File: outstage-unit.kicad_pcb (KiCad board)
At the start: 2 copper layers, 100 x 220 mm, 76 parts, among them J101 Conn_01x06_Socket, M101 Fan, Q201 DNLS350E, Q202 DPLS350E, Q203 TIP41C, Q204 TIP42C, Q301 DNLS350E, Q302 DPLS350E, Q303 TIP41C, Q304 TIP42C, Q401 DNLS350E, Q402 DPLS350E, Q403 TIP41C, Q404 TIP42C, Q501 DNLS350E, Q502 DPLS350E, Q503 TIP41C, Q504 TIP42C, Q601 DNLS350E, Q602 DPLS350E, Q603 TIP41C, Q604 TIP42C, Q701 DNLS350E, Q702 DPLS350E, Q703 TIP41C, Q704 TIP42C

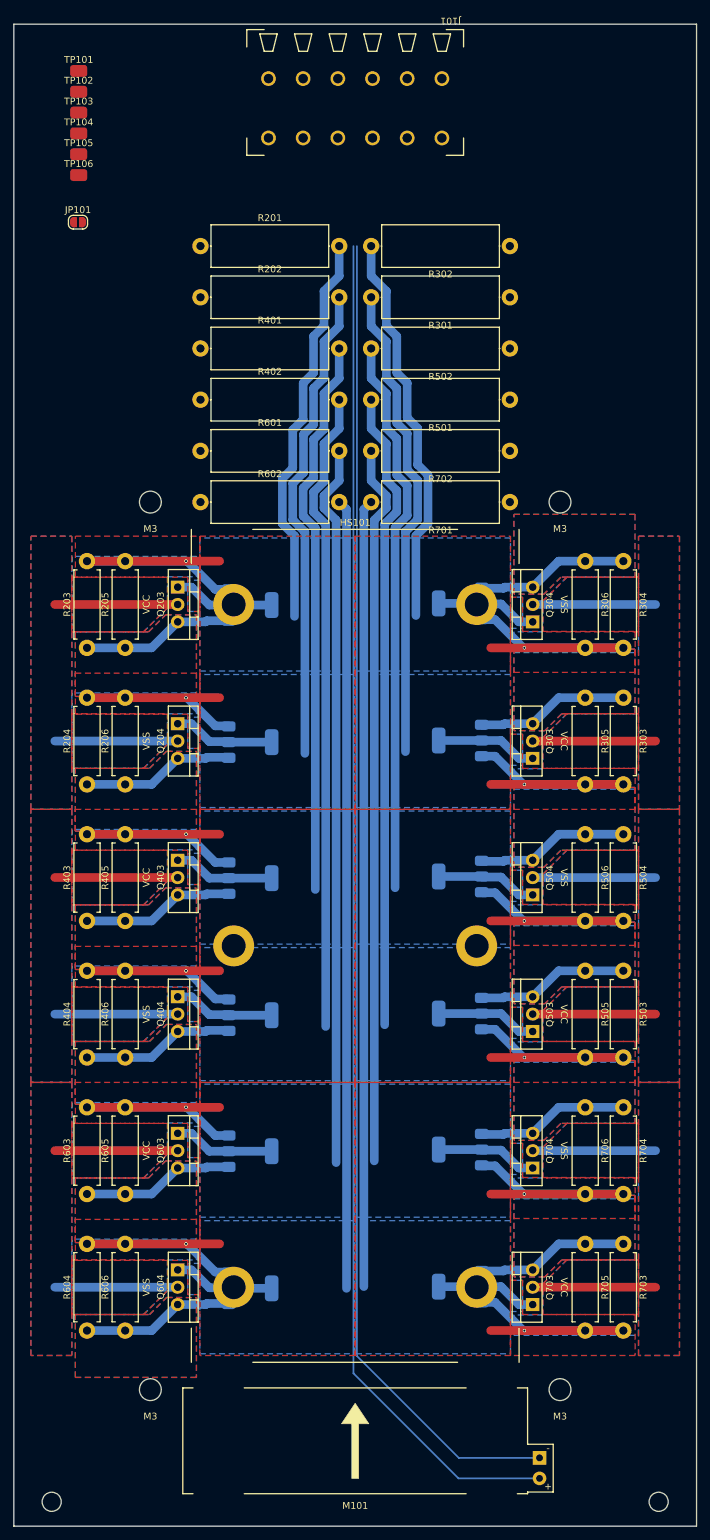
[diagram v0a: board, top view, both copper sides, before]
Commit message: add pcb sub circuit outstage-unit
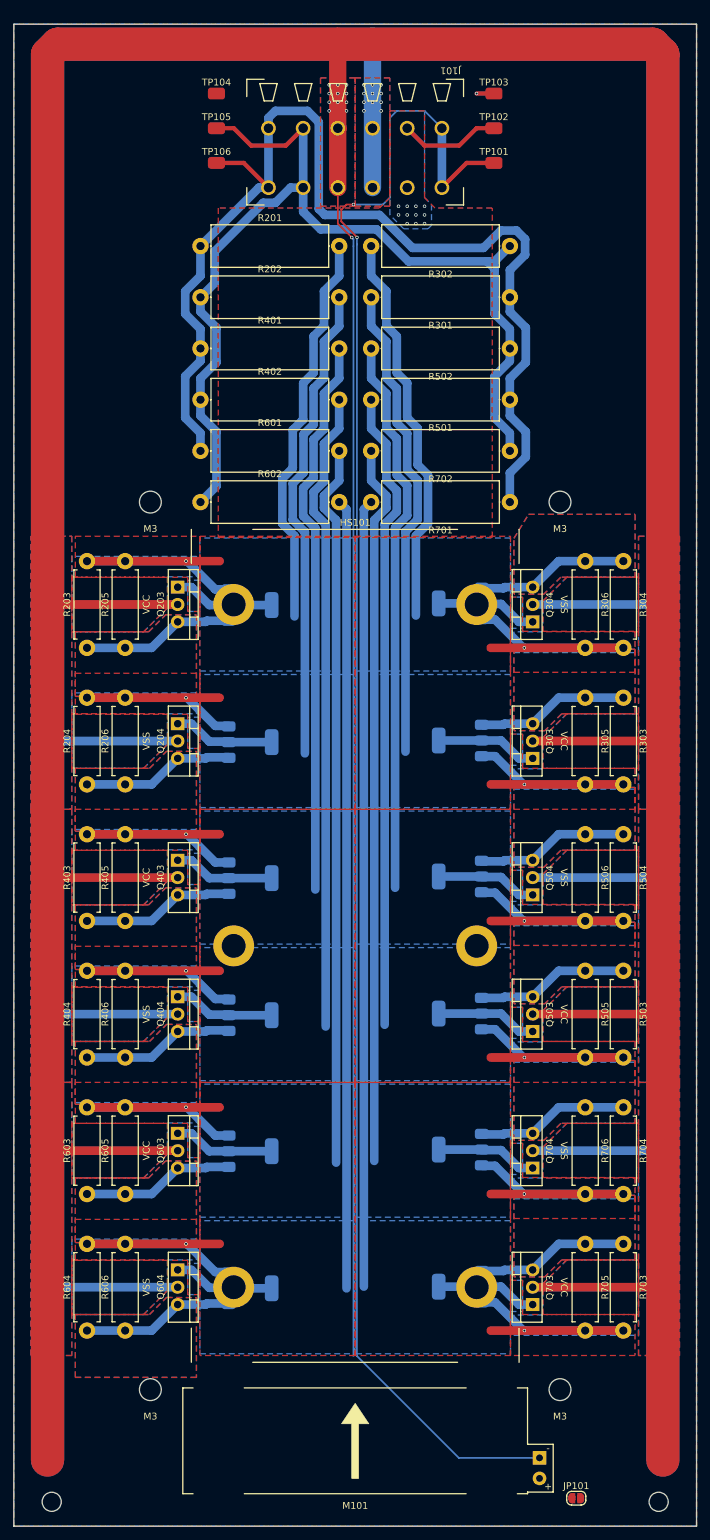
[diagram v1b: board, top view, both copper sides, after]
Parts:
- moved JP101 200.6 mm to (117.4, 235.9)
- moved TP101 62.3 mm to (105.3, 40.3)
- moved TP102 61.1 mm to (105.3, 35.2)
- moved TP103 60.9 mm to (105.3, 30.2)
- moved TP104 21.0 mm to (64.7, 30.2)
- moved TP105 20.5 mm to (64.7, 35.2)
- moved TP106 20.3 mm to (64.7, 40.3)
- moved J101 7.27 mm to (97.7, 43.9)
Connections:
- J101 pad 3: /v_in+ -> /-5V
- J101 pad 4: /v_in- -> /+10V
- J101 pad 5: /+10V -> /v_in-
- J101 pad 6: /-5V -> /v_in+
- TP103 pad 1: /v_in+ -> /-5V
- TP104 pad 1: /v_in- -> /+10V
- TP105 pad 1: /+10V -> /v_in-
- TP106 pad 1: /-5V -> /v_in+
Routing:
- net /+10V: track 108.0 -> 804.2 mm, vias 0 -> 12
- net /-5V: track 108.0 -> 634.7 mm, vias 0 -> 12
- net Net-(JP101-B): track 198.7 -> 0.00 mm
- net /v_in+: track 0.00 -> 165.4 mm
- net /v_in-: track 0.00 -> 151.6 mm
- net /GND: track 195.5 -> 248.2 mm, vias 0 -> 2
- net /v_out: track 502.7 -> 517.5 mm, vias 12 -> 23
- added copper zone on B.Cu, net /+10V
- added copper zone on F.Cu, net /-5V
- added copper zone on B.Cu, net /v_out

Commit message: edit heatsink mounting holes position, fix copper pour
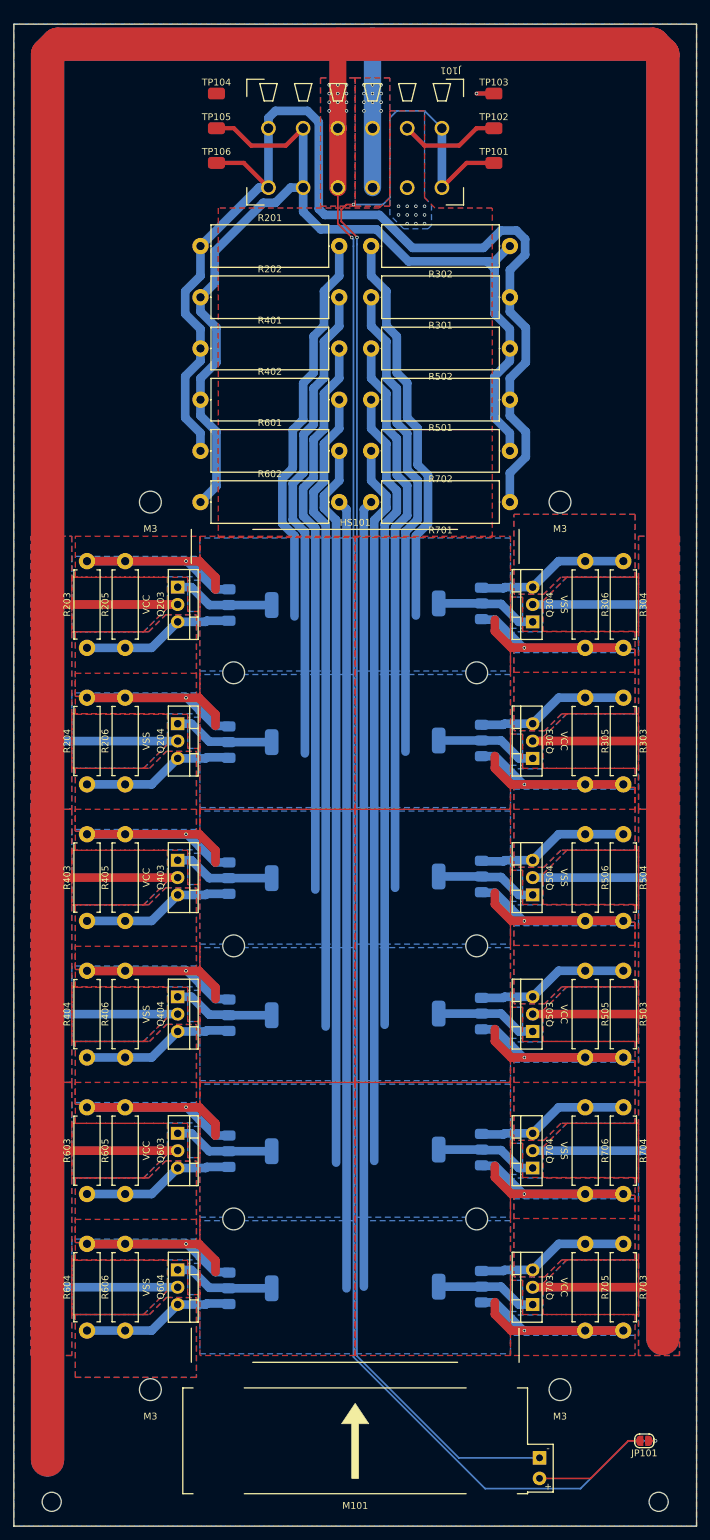
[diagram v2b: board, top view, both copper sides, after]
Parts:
- moved JP101 13.0 mm to (127.3, 227.5), turned to 180 degrees
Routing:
- net /+10V: track 804.2 -> 842.8 mm, vias 12 -> 13
- net /v_out: track 517.5 -> 542.9 mm
- net /-5V: track 634.7 -> 616.9 mm
- net Net-(JP101-B): track 0.00 -> 17.0 mm
